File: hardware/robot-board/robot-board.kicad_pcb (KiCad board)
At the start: 4 copper layers, 69 x 99 mm, 132 parts, among them J1 Conn_01x09_Pin, J10 1x2_Screw, J11 1x2_Screw, J2 Barrel_Jack, J3 USB_C_Receptacle_USB2.0_14P, J4 Conn_01x03_Pin, J5 Conn_01x03_Pin, J6 Conn_01x03_Pin, J7 Conn_01x03_Pin, J8 1x2_Screw, J9 1x2_Screw, Q1 BSS138, Q2 BSS138, Q3 BSS138, Q4 BSS138, Q5 BSS138, Q6 BSS138, Q7 BSS138, Q8 BSS138, SW1 SW_SPST, SW2 SW_SPST, U1 ESP32-S3-WROOM-1, U2 LMR51450, U3 LMR51450, U4 TVS1400DRV, U5 TPS552892, U6 DRV8835, U7 DRV8835, U8 XL-SA3391SRWC, U9 STP08CP05M

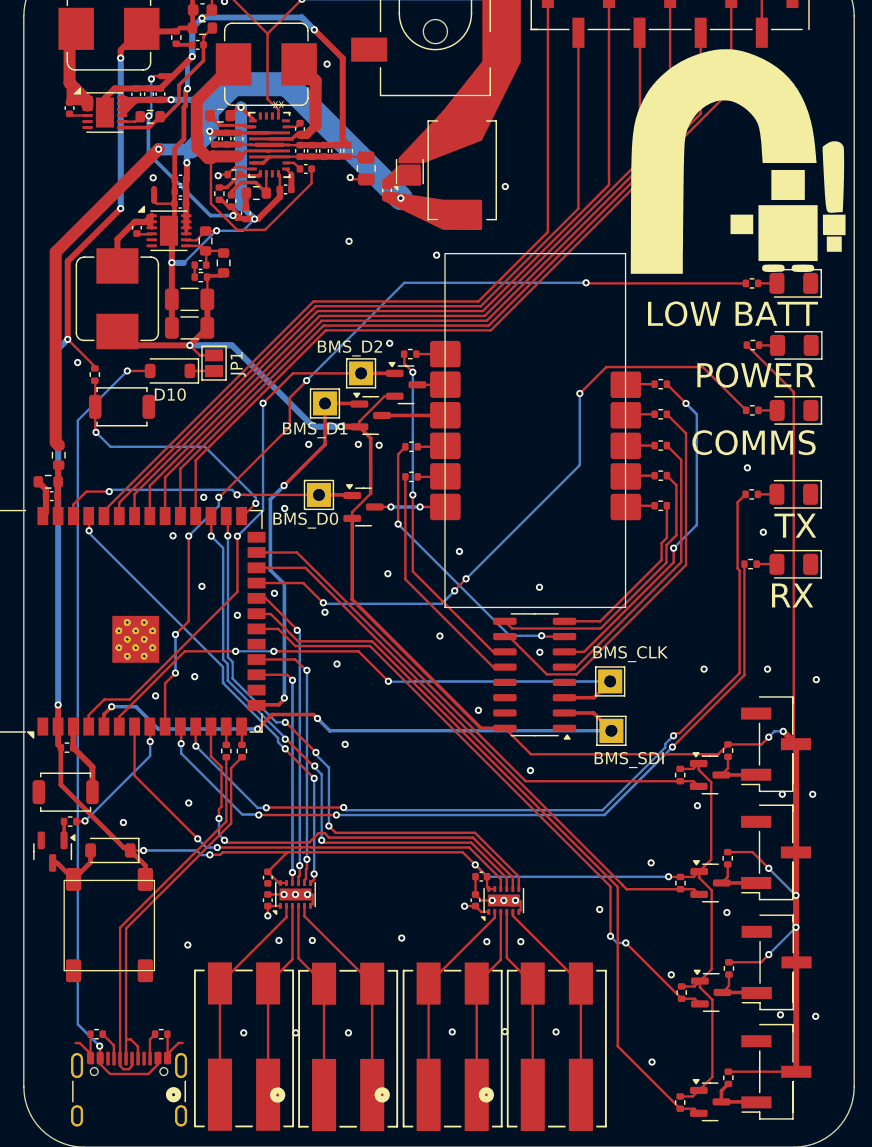
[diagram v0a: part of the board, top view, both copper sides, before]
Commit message: changed display driver
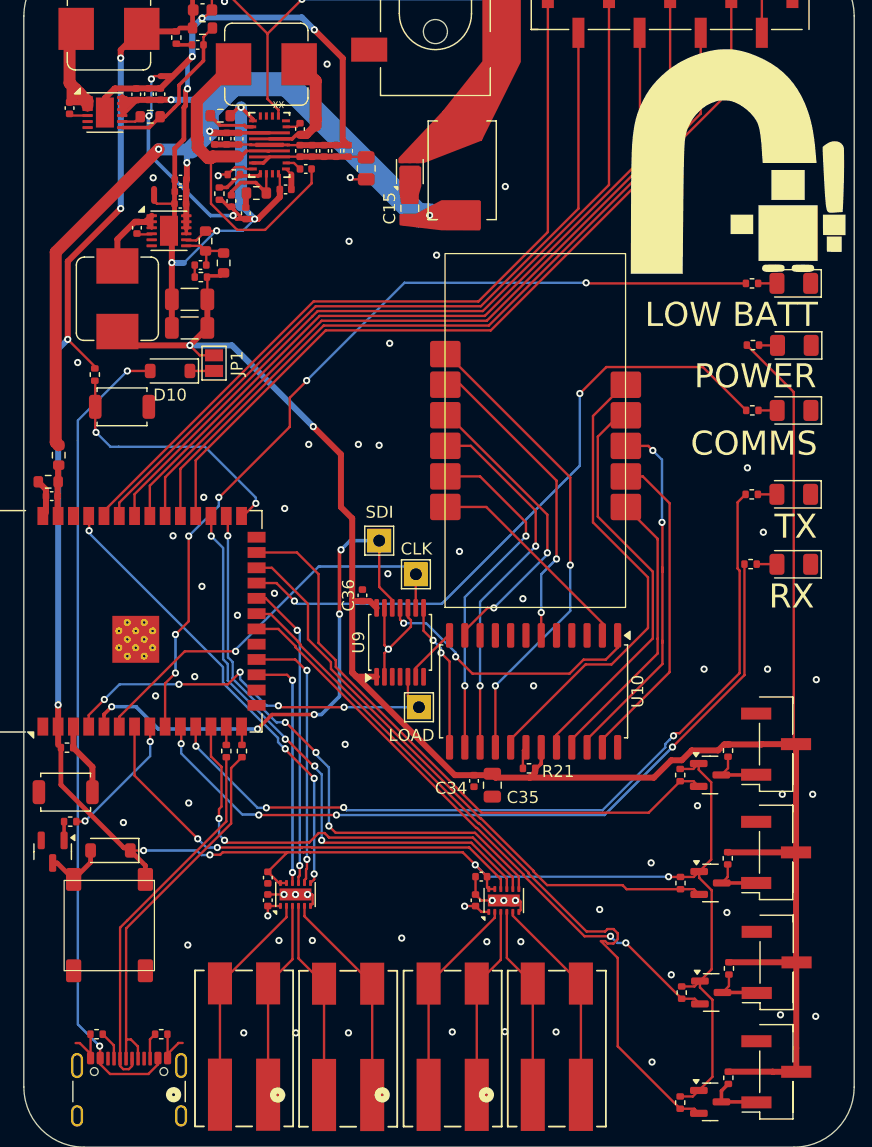
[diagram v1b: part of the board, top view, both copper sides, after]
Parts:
- removed Q6, Q7, Q8: BSS138, Package_TO_SOT_SMD:SOT-23
- removed R34, R35, R36, R37, R38, R39, R40, R41: 33R, Resistor_SMD:R_0402_1005Metric
- removed TP2: D0, TestPoint:TestPoint_THTPad_2.0x2.0mm_Drill1.0mm
- removed TP3: D1, TestPoint:TestPoint_THTPad_2.0x2.0mm_Drill1.0mm
- added C34: 0.1uF, Capacitor_SMD:C_0402_1005Metric, F.Cu at (73.4, 121.6)
- added C35: 10uF, Capacitor_SMD:C_0805_2012Metric, F.Cu at (74.9, 121.9)
- added C36: 0.1uF, Capacitor_SMD:C_0402_1005Metric, F.Cu at (64.1, 106.1)
- added R21: 33k, Resistor_SMD:R_0402_1005Metric, F.Cu at (78.0, 120.5)
- added U10: MAX7219, Package_SO:SOIC-24W_7.5x15.4mm_P1.27mm, F.Cu at (78.4, 114.1)
- C15: footprint Capacitor_SMD:C_0402_1005Metric -> Capacitor_SMD:C_0805_2012Metric
- U9: value STP08CP05M -> 74AHCT125; footprint Package_SO:SOIC-16_3.9x9.9mm_P1.27mm -> Package_SO:TSSOP-14_4.4x5mm_P0.65mm
- moved TP4 28.2 mm to (68.8, 115.4)
- moved TP5 24.9 mm to (65.5, 101.6)
- moved TP6 18.4 mm to (68.6, 104.4)
- moved U9 11.5 mm to (67.3, 110.1), turned to 90 degrees
- moved C15 2.40 mm to (68.1, 74.0)
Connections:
- TP4 pad 1: /BMS_D2 -> /BMS_LOAD
- U1 pad 15: /BMS_D1 -> unconnected-(U1-IO3-Pad15)
- U1 pad 38: /BMS_D0 -> unconnected-(U1-IO2-Pad38)
- U1 pad 4: /BMS_D2 -> /BMS_LOAD
- U9 pad 1: GND -> +5V
- U9 pad 10: Net-(U9-~{OUT5}) -> GND
- U9 pad 12: Net-(U9-~{OUT7}) -> /BMS_SDI
- U9 pad 14: unconnected-(U9-SDO-Pad14) -> +5V
- U9 pad 2: /BMS_SDI -> GND
- U9 pad 3: /BMS_CLK -> unconnected-(U9-Pad3)
- U9 pad 4: unconnected-(U9-LE-Pad4) -> GND
- U9 pad 5: Net-(U9-~{OUT0}) -> /BMS_LOAD
- U9 pad 7: Net-(U9-~{OUT2}) -> GND
- U9 pad 9: Net-(U9-~{OUT4}) -> /BMS_CLK
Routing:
- net /BMS_D2: track 46.1 -> 0.00 mm, vias 2 -> 0
- net Net-(U10-SEG_B): track 2.40 -> 39.6 mm, vias 0 -> 2
- net Net-(U10-SEG_G): track 2.41 -> 39.3 mm
- net /BMS_LOAD: track 0.00 -> 34.3 mm, vias 0 -> 5
- net Net-(U9-~{OUT5}): track 33.3 -> 0.00 mm
- net /BMS_D1: track 32.3 -> 0.00 mm, vias 2 -> 0
- net Net-(U10-SEG_C): track 2.43 -> 34.2 mm
- net Net-(U10-SEG_F): track 2.33 -> 31.4 mm, vias 0 -> 2
- net Net-(U10-SEG_DP): track 2.40 -> 30.2 mm, vias 0 -> 2
- net Net-(U10-SEG_A): track 2.32 -> 29.1 mm, vias 0 -> 2
- net Net-(U10-SEG_D): track 2.42 -> 27.2 mm
- net /BMS_D0: track 24.8 -> 0.00 mm, vias 2 -> 0
- net Net-(U9-~{OUT2}): track 24.4 -> 0.00 mm, vias 2 -> 0
- net Net-(U10-LOAD): track 28.8 -> 4.67 mm, vias 2 -> 0
- net Net-(U9-~{OUT4}): track 23.8 -> 0.00 mm
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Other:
- board text added: "CLK"
- board text added: "LOAD"
- board text added: "SDI"
- board text removed: "BMS_CLK"
- board text removed: "BMS_D0"
- board text removed: "BMS_D1"
- board text removed: "BMS_D2"
- board text removed: "BMS_SDI"

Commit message: should be final
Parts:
- added H1: MountingHole, MountingHole:MountingHole_3.2mm_M3, F.Cu at (94.1, 68.5)
- added H2: MountingHole, MountingHole:MountingHole_3.2mm_M3, F.Cu at (88.8, 143.3)
- added H3: MountingHole, MountingHole:MountingHole_3.2mm_M3, F.Cu at (41.0, 71.5)
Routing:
- net GND: track 34.7 -> 46.7 mm, vias 64 -> 69
- net +5V: track 181.0 -> 185.5 mm, vias 2 -> 4
- net /SERVO3_PWM: track 50.6 -> 54.8 mm
- net /SERVO2_PWM: track 50.1 -> 54.2 mm
- net /SERVO1_PWM: track 49.8 -> 53.8 mm
- net /SERVO0_PWM: track 62.3 -> 65.6 mm
- net Vprot: track 84.7 -> 85.8 mm
- net /MOTOR1_PWM: track 37.0 -> 36.0 mm
- net /LF0: track 69.9 -> 70.8 mm
- net +3V3: track 241.6 -> 242.2 mm

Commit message: gerbers final
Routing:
- net /LBAT_LED: track 73.6 -> 74.6 mm
- net /LF0: track 70.8 -> 69.9 mm
- net Net-(U10-SEG_A): track 29.1 -> 29.8 mm
- net Vprot: vias 5 -> 6
- net GND: vias 69 -> 72
